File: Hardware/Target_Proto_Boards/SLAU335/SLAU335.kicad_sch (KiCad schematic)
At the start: 37 parts, among them J1 USB_B_Micro, J10 GND, J11 +5V, J12 GND, J13 VSEL, J2 LogicAna, J3 DEBUG, J4 PORT1, J5 LED_P2.2, J6 PORT2, J7 JTAG/SBW, J8 AIN, J9 VCC, SW1 TL-2203, SW2 RESET, U1 MSP430I2041TPW, U2 AMS1117-3.3

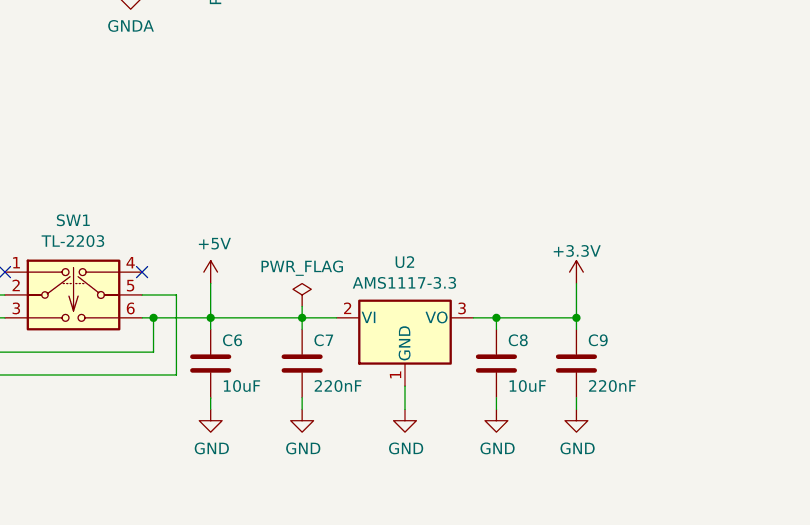
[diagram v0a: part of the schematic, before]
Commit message: Fixed regulator part#
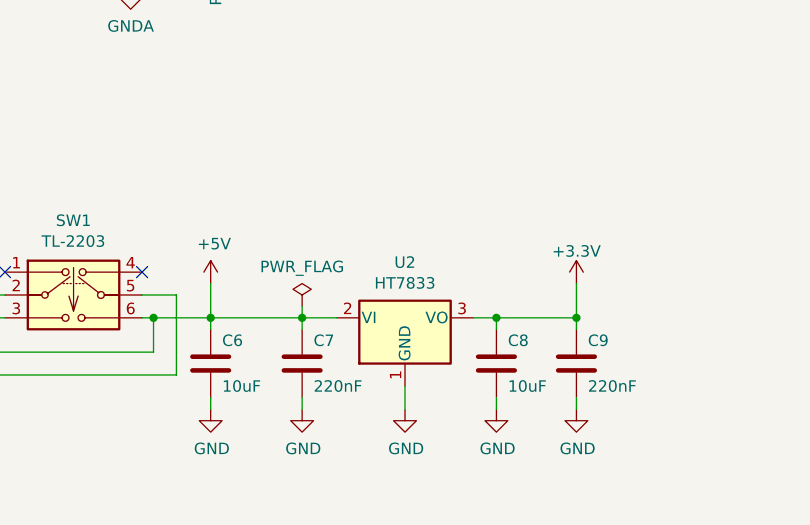
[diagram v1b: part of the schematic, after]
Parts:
- U2: value AMS1117-3.3 -> HT7833
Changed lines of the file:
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@@
     (in_bom yes) (on_board yes)
     (property "Reference" "U2" (id 0) (at 87.63 162.7632 0))
-    (property "Value" "AMS1117-3.3" (id 1) (at 87.63 165.0746 0))
+    (property "Value" "HT7833" (id 1) (at 87.63 165.0746 0))
     (property "Footprint" "Package_TO_SOT_SMD:SOT-89-3_Handsoldering" (id 2) (at 87.63 163.83 0)
       (effects (font (size 1.27 1.27)) hide)
@@
     )
     (path "/00000000-0000-0000-0000-0000610e48b7"
-      (reference "U2") (unit 1) (value "AMS1117-3.3") (footprint "Package_TO_SOT_SMD:SOT-89-3_Handsoldering")
-    )
-  )
+      (reference "U2") (unit 1) (value "HT7833") (footprint "Package_TO_SOT_SMD:SOT-89-3_Handsoldering")
+    )
+  )
